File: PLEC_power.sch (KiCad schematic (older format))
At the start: 16 parts, among them K1 PB1167, U1 LM1085-5.0, U2 LM1085-3.3

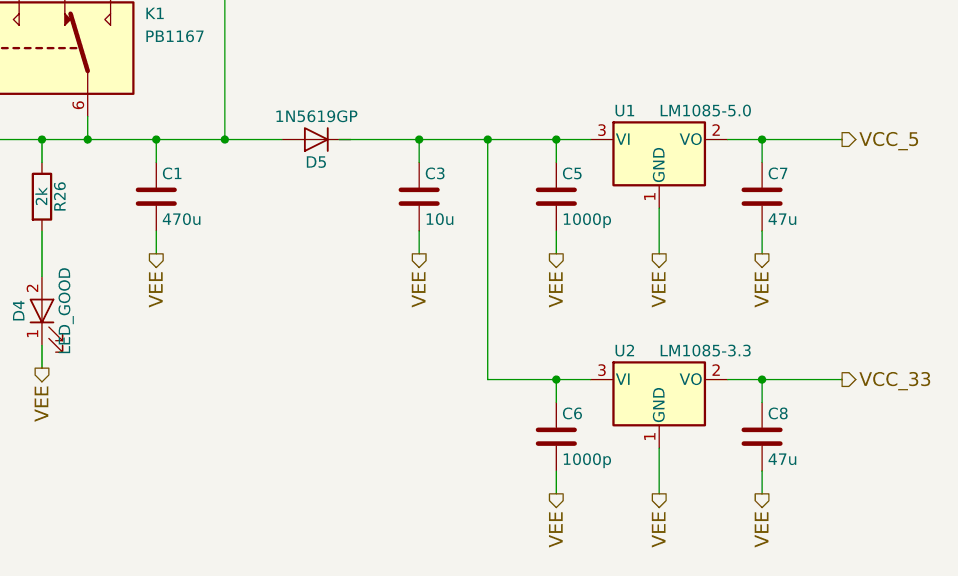
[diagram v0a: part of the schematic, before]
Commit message: Almost done with layout; need to rearrange uC pins
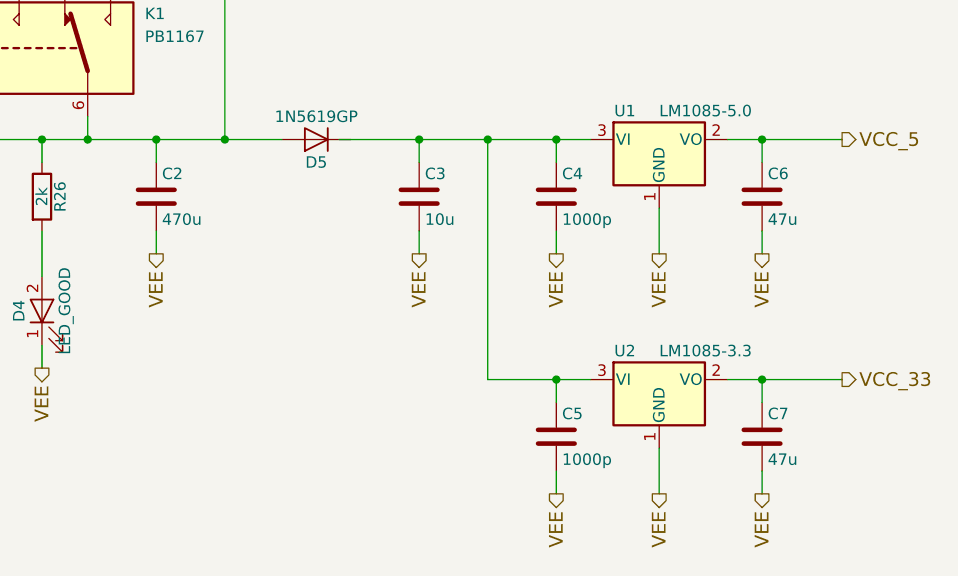
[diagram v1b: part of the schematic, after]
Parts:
- renumbered C1 to C2, C5 to C4, C6 to C5, C7 to C6, C8 to C7
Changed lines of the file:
@@
 Connection ~ 7300 2950
 $Comp
-L C C5
+L C C4
 U 1 1 5A71B3AD
 P 6400 3200
-F 0 "C5" H 6425 3300 50  0000 L CNN
+F 0 "C4" H 6425 3300 50  0000 L CNN
 F 1 "1000p" H 6425 3100 50  0000 L CNN
 F 2 "PLEC:THTt_100Px200Lx125Wx200H_1000p" H 6438 3050 50  0001 C CNN
@@
 Connection ~ 7300 4000
 $Comp
-L C C6
+L C C5
 U 1 1 5A75EBF4
 P 6400 4250
-F 0 "C6" H 6425 4350 50  0000 L CNN
+F 0 "C5" H 6425 4350 50  0000 L CNN
 F 1 "1000p" H 6425 4150 50  0000 L CNN
 F 2 "PLEC:THTt_100Px200Lx125Wx200H_1000p" H 6438 4100 50  0001 C CNN
@@
 	4950 2250 5250 2250
 $Comp
-L C C7
+L C C6
 U 1 1 5A765DE6
 P 7300 3200
-F 0 "C7" H 7325 3300 50  0000 L CNN
+F 0 "C6" H 7325 3300 50  0000 L CNN
 F 1 "47u" H 7325 3100 50  0000 L CNN
 F 2 "PLEC:THTm_2Px4Dx12H_47u" H 7338 3050 50  0001 C CNN
@@
 $EndComp
 $Comp
-L C C8
+L C C7
 U 1 1 5A765E43
 P 7300 4250
-F 0 "C8" H 7325 4350 50  0000 L CNN
+F 0 "C7" H 7325 4350 50  0000 L CNN
 F 1 "47u" H 7325 4150 50  0000 L CNN
 F 2 "PLEC:THTm_2Px4Dx12H_47u" H 7338 4100 50  0001 C CNN
@@
 	5450 2950 6550 2950
 $Comp
-L C C1
+L C C2
 U 1 1 5A761A80
 P 4650 3200
-F 0 "C1" H 4675 3300 50  0000 L CNN
+F 0 "C2" H 4675 3300 50  0000 L CNN
 F 1 "470u" H 4675 3100 50  0000 L CNN
 F 2 "PLEC:THTm_5Px8Dx22H__470u" H 4688 3050 50  0001 C CNN

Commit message: Finished PCB with no errors
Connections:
- net V9_DIODE: now reaches C3.1, C4.1, C5.1, U1.3 (VI), U2.3 (VI)
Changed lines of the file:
@@
 	4650 3050 4650 2950
 Connection ~ 4650 2950
+Text Label 5700 2950 0    60   ~ 0
+V9_DIODE
 $EndSCHEMATC

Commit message: Replaced solid state relays with NPN Darlingtons
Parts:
- removed C4: 1000p, PLEC:THTt_100Px200Lx125Wx200H_1000p, symbol C
- removed D2: D_Zener, Diodes_THT:D_DO-201AD_P15.24mm_Horizontal, symbol D_Zener
- removed D3: LED_OL, LEDs:LED_D3.0mm_FlatTop, symbol LED
- removed K1: PB1167, PLEC:PB1167, symbol IM00
- R25: value 600 -> 2k; footprint Resistors_THT:R_Axial_DIN0414_L11.9mm_D4.5mm_P20.32mm_Horizontal -> Resistors_THT:R_Axial_DIN0204_L3.6mm_D1.6mm_P5.08mm_Horizontal
- U1: symbol LM1085-5.0 -> LM1085-5.0-RESCUE-PLEC
- U2: symbol LM1085-3.3 -> LM1085-3.3-RESCUE-PLEC
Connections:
- net VCC_9_OL is gone; now on net VBAT: C2.1, D5.2 (A), R26.1
- net V9_DIODE: now also D5.1 (K)
- net VBAT: now reaches R25.1
- net VEE renamed GND
- no-connect marks 2 -> 0
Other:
- note added: "Diode prevents arming event from\npulling voltage from LDOs\n(Another BFC near relays)"
- note added: "LM1085\nMaximum output: 3A\n5V max drain: 0.300A (Teensy) + 0.019A (HXS2) + 0.003A (NBP) = 0.325A \n3V max drain: 0.230A (XBee) = 0.230A"
- moved on the sheet: C5, D1
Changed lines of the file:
@@
 EESchema Schematic File Version 2
+LIBS:PLEC-rescue
 LIBS:power
 LIBS:device
@@
 LIBS:PLEC
 LIBS:cap_470u
+LIBS:BDW42G
 LIBS:PLEC-cache
 EELAYER 25 0
@@
 Wire Wire Line
 	7150 2950 7650 2950
+Connection ~ 7300 2950
 Connection ~ 6400 2950
-Connection ~ 7300 2950
-$Comp
-L C C4
-U 1 1 5A71B3AD
-P 6400 3200
-F 0 "C4" H 6425 3300 50  0000 L CNN
-F 1 "1000p" H 6425 3100 50  0000 L CNN
-F 2 "PLEC:THTt_100Px200Lx125Wx200H_1000p" H 6438 3050 50  0001 C CNN
-F 3 "" H 6400 3200 50  0001 C CNN
-	1    6400 3200
-	1    0    0    -1
-$EndComp
-Connection ~ 6100 2950
 $Comp
 L C C3
@@
 $EndComp
 $Comp
-L LM1085-3.3 U2
+L LM1085-3.3-RESCUE-PLEC U2
 U 1 1 5A71B3E2
 P 6850 4000
+AR Path="/5A71B3E2" Ref="U2"  Part="1"
+AR Path="/5A71AC48/5A71B3E2" Ref="U2"  Part="1"
 F 0 "U2" H 6700 4125 50  0000 C CNN
 F 1 "LM1085-3.3" H 6850 4125 50  0000 L CNN
@@
 $EndComp
 $Comp
-L LM1085-5.0 U1
+L LM1085-5.0-RESCUE-PLEC U1
 U 1 1 5A71B3E9
 P 6850 2950
@@
 Text HLabel 7650 2950 2    60   Output ~ 0
 VCC_5
-Text HLabel 5800 3450 3    60   Output ~ 0
-VEE
-Text HLabel 6400 3450 3    60   Output ~ 0
-VEE
-Text HLabel 6850 3450 3    60   Output ~ 0
-VEE
-Text HLabel 7300 3450 3    60   Output ~ 0
-VEE
-Text HLabel 3300 1750 0    60   Input ~ 0
-VCC_9
-$Comp
-L IM00 K1
-U 1 1 5A75DE52
-P 3750 2550
-F 0 "K1" H 4600 2700 50  0000 L CNN
-F 1 "PB1167" H 4600 2600 50  0000 L CNN
-F 2 "PLEC:PB1167" H 3750 2550 50  0001 C CNN
-F 3 "" H 3750 2550 50  0001 C CNN
-	1    3750 2550
-	1    0    0    -1
-$EndComp
-$Comp
-L D_Zener D2
-U 1 1 5A75DE91
-P 3550 2000
-F 0 "D2" H 3550 2100 50  0000 C CNN
-F 1 "D_Zener" H 3550 1900 50  0000 C CNN
-F 2 "Diodes_THT:D_DO-201AD_P15.24mm_Horizontal" H 3550 2000 50  0001 C CNN
-F 3 "" H 3550 2000 50  0001 C CNN
-	1    3550 2000
-	0    1    1    0
-$EndComp
-Wire Wire Line
-	3550 2250 3550 2150
+Text HLabel 3000 2350 0    60   Input ~ 0
+VBAT
 $Comp
 L R R25
@@
 P 3550 3200
 F 0 "R25" V 3630 3200 50  0000 C CNN
-F 1 "600" V 3550 3200 50  0000 C CNN
-F 2 "Resistors_THT:R_Axial_DIN0414_L11.9mm_D4.5mm_P20.32mm_Horizontal" V 3480 3200 50  0001 C CNN
+F 1 "2k" V 3550 3200 50  0000 C CNN
+F 2 "Resistors_THT:R_Axial_DIN0204_L3.6mm_D1.6mm_P5.08mm_Horizontal" V 3480 3200 50  0001 C CNN
 F 3 "" H 3550 3200 50  0001 C CNN
 	1    3550 3200
@@
 $EndComp
 Wire Wire Line
-	3550 3050 3550 2850
-Text HLabel 3550 3950 3    60   Output ~ 0
-VEE
-Wire Wire Line
-	3300 1750 4250 1750
-Wire Wire Line
-	3850 1750 3850 2250
-Wire Wire Line
-	4250 1750 4250 2250
-Connection ~ 3850 1750
-NoConn ~ 4050 2250
-NoConn ~ 4450 2250
-Wire Wire Line
-	3950 2850 3950 2950
-Wire Wire Line
-	4350 2950 4350 2850
-Connection ~ 4350 2950
-$Comp
-L LED D3
-U 1 1 5A75E59A
-P 3550 3700
-F 0 "D3" H 3550 3800 50  0000 C CNN
-F 1 "LED_OL" H 3550 3600 50  0000 C CNN
-F 2 "LEDs:LED_D3.0mm_FlatTop" H 3550 3700 50  0001 C CNN
-F 3 "" H 3550 3700 50  0001 C CNN
-	1    3550 3700
-	0    -1   -1   0
-$EndComp
-Wire Wire Line
-	3550 3350 3550 3550
-Wire Wire Line
-	3550 3850 3550 3950
+	3550 2350 3550 3050
+Wire Wire Line
+	3000 2350 3950 2350
+Wire Wire Line
+	3950 2350 3950 2950
+Connection ~ 3550 2350
 Wire Wire Line
 	5800 2950 5800 3050
 Wire Wire Line
-	6400 2950 6400 3050
-Wire Wire Line
-	5800 3450 5800 3350
-Wire Wire Line
-	6400 3450 6400 3350
+	5800 3950 5800 3350
 Wire Wire Line
 	7300 3450 7300 3350
@@
 Wire Wire Line
 	6850 3450 6850 3250
-Connection ~ 6400 4000
+Connection ~ 6400 3450
 Connection ~ 7300 4000
 $Comp
 L C C5
 U 1 1 5A75EBF4
-P 6400 4250
-F 0 "C5" H 6425 4350 50  0000 L CNN
-F 1 "1000p" H 6425 4150 50  0000 L CNN
-F 2 "PLEC:THTt_100Px200Lx125Wx200H_1000p" H 6438 4100 50  0001 C CNN
-F 3 "" H 6400 4250 50  0001 C CNN
-	1    6400 4250
-	1    0    0    -1
-$EndComp
-Text HLabel 6400 4500 3    60   Output ~ 0
-VEE
-Text HLabel 6850 4500 3    60   Output ~ 0
-VEE
-Text HLabel 7300 4500 3    60   Output ~ 0
-VEE
-Wire Wire Line
-	6400 4000 6400 4100
-Wire Wire Line
-	6400 4500 6400 4400
+P 6100 3700
+F 0 "C5" H 6125 3800 50  0000 L CNN
+F 1 "1000p" H 6125 3600 50  0000 L CNN
+F 2 "PLEC:THTt_100Px200Lx125Wx200H_1000p" H 6138 3550 50  0001 C CNN
+F 3 "" H 6100 3700 50  0001 C CNN
+	1    6100 3700
+	1    0    0    -1
+$EndComp
+Wire Wire Line
+	6100 3950 6100 3850
 Wire Wire Line
 	7300 4500 7300 4400
@@
 	7150 4000 7650 4000
 Wire Wire Line
-	6100 4000 6550 4000
-Wire Wire Line
-	6100 2950 6100 4000
+	6100 3450 6400 3450
+Wire Wire Line
+	6400 2950 6400 4000
 Connection ~ 5800 2950
 $Comp
@@
 	1    0    0    -1
 $EndComp
-Text HLabel 4150 3950 3    60   Output ~ 0
-VEE
 $Comp
 L LED D4
@@
 	4150 3050 4150 2950
 Connection ~ 4150 2950
-Text HLabel 2950 3450 0    60   Input ~ 0
-VEE
 $Comp
 L LED D1
 U 1 1 5A75F790
-P 3200 3450
-F 0 "D1" H 3200 3550 50  0000 C CNN
-F 1 "LED_RP" H 3200 3350 50  0000 C CNN
-F 2 "LEDs:LED_D3.0mm_FlatTop" H 3200 3450 50  0001 C CNN
-F 3 "" H 3200 3450 50  0001 C CNN
-	1    3200 3450
-	-1   0    0    1
-$EndComp
-Wire Wire Line
-	2950 3450 3050 3450
-Wire Wire Line
-	3350 3450 3550 3450
-Connection ~ 3550 3450
-Text HLabel 5250 2250 2    60   Output ~ 0
-VCC_9_OL
-Wire Wire Line
-	4950 2250 5250 2250
+P 3550 3700
+F 0 "D1" H 3550 3800 50  0000 C CNN
+F 1 "LED_RP" H 3550 3600 50  0000 C CNN
+F 2 "LEDs:LED_D3.0mm_FlatTop" H 3550 3700 50  0001 C CNN
+F 3 "" H 3550 3700 50  0001 C CNN
+	1    3550 3700
+	0    1    1    0
+$EndComp
+Wire Wire Line
+	3550 3950 3550 3850
+Wire Wire Line
+	3550 3550 3550 3350
 $Comp
 L C C6
@@
 	1    0    0    -1
 $EndComp
-Wire Wire Line
-	3550 1850 3550 1750
-Connection ~ 3550 1750
 $Comp
 L D D5
@@
 	3950 2950 5200 2950
 Wire Wire Line
-	4950 2950 4950 2250
-Connection ~ 4950 2950
-Wire Wire Line
-	5450 2950 6550 2950
+	5500 2950 6550 2950
 $Comp
 L C C2
@@
 	1    0    0    -1
 $EndComp
-Text HLabel 4650 3450 3    60   Output ~ 0
-VEE
-Wire Wire Line
-	4650 3450 4650 3350
+Wire Wire Line
+	4650 3950 4650 3350
 Wire Wire Line
 	4650 3050 4650 2950
@@
 Text Label 5700 2950 0    60   ~ 0
 V9_DIODE
+$Comp
+L GND #PWR017
+U 1 1 5A872C88
+P 3550 3950
+F 0 "#PWR017" H 3550 3700 50  0001 C CNN
+F 1 "GND" H 3550 3800 50  0000 C CNN
+F 2 "" H 3550 3950 50  0001 C CNN
+F 3 "" H 3550 3950 50  0001 C CNN
+	1    3550 3950
+	1    0    0    -1
+$EndComp
+$Comp
+L GND #PWR018
+U 1 1 5A872D50
+P 4150 3950
+F 0 "#PWR018" H 4150 3700 50  0001 C CNN
+F 1 "GND" H 4150 3800 50  0000 C CNN
+F 2 "" H 4150 3950 50  0001 C CNN
+F 3 "" H 4150 3950 50  0001 C CNN
+	1    4150 3950
+	1    0    0    -1
+$EndComp
+$Comp
+L GND #PWR019
+U 1 1 5A872DA6
+P 4650 3950
+F 0 "#PWR019" H 4650 3700 50  0001 C CNN
+F 1 "GND" H 4650 3800 50  0000 C CNN
+F 2 "" H 4650 3950 50  0001 C CNN
+F 3 "" H 4650 3950 50  0001 C CNN
+	1    4650 3950
+	1    0    0    -1
+$EndComp
+$Comp
+L GND #PWR020
+U 1 1 5A872DD8
+P 5800 3950
+F 0 "#PWR020" H 5800 3700 50  0001 C CNN
+F 1 "GND" H 5800 3800 50  0000 C CNN
+F 2 "" H 5800 3950 50  0001 C CNN
+F 3 "" H 5800 3950 50  0001 C CNN
+	1    5800 3950
+	1    0    0    -1
+$EndComp
+$Comp
+L GND #PWR021
+U 1 1 5A872E3C
+P 6850 3450
+F 0 "#PWR021" H 6850 3200 50  0001 C CNN
+F 1 "GND" H 6850 3300 50  0000 C CNN
+F 2 "" H 6850 3450 50  0001 C CNN
+F 3 "" H 6850 3450 50  0001 C CNN
+	1    6850 3450
+	1    0    0    -1
+$EndComp
+$Comp
+L GND #PWR022
+U 1 1 5A872E6E
+P 7300 3450
+F 0 "#PWR022" H 7300 3200 50  0001 C CNN
+F 1 "GND" H 7300 3300 50  0000 C CNN
+F 2 "" H 7300 3450 50  0001 C CNN
+F 3 "" H 7300 3450 50  0001 C CNN
+	1    7300 3450
+	1    0    0    -1
+$EndComp
+$Comp
+L GND #PWR023
+U 1 1 5A872EA0
+P 6100 3950
+F 0 "#PWR023" H 6100 3700 50  0001 C CNN
+F 1 "GND" H 6100 3800 50  0000 C CNN
+F 2 "" H 6100 3950 50  0001 C CNN
+F 3 "" H 6100 3950 50  0001 C CNN
+	1    6100 3950
+	1    0    0    -1
+$EndComp
+$Comp
+L GND #PWR024
+U 1 1 5A872ED2
+P 6850 4500
+F 0 "#PWR024" H 6850 4250 50  0001 C CNN
+F 1 "GND" H 6850 4350 50  0000 C CNN
+F 2 "" H 6850 4500 50  0001 C CNN
+F 3 "" H 6850 4500 50  0001 C CNN
+	1    6850 4500
+	1    0    0    -1
+$EndComp
+$Comp
+L GND #PWR025
+U 1 1 5A872F04
+P 7300 4500
+F 0 "#PWR025" H 7300 4250 50  0001 C CNN
+F 1 "GND" H 7300 4350 50  0000 C CNN
+F 2 "" H 7300 4500 50  0001 C CNN
+F 3 "" H 7300 4500 50  0001 C CNN
+	1    7300 4500
+	1    0    0    -1
+$EndComp
+Text Notes 5600 2750 2    60   ~ 0
+Diode prevents arming event from\npulling voltage from LDOs\n(Another BFC near relays)
+Text Notes 7650 3600 0    60   ~ 0
+LM1085\nMaximum output: 3A\n5V max drain: 0.300A (Teensy) + 0.019A (HXS2) + 0.003A (NBP) = 0.325A \n3V max drain: 0.230A (XBee) = 0.230A
+Wire Wire Line
+	6400 4000 6550 4000
+Wire Wire Line
+	6100 3550 6100 3450
 $EndSCHEMATC
